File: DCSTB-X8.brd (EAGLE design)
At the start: 29 x 87 mm, 6 parts

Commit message: Changed board texts. Generated CAM files. Generated PDF schematics.
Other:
- board text added: "DCSTB-X8-0010 (c) Andriy Golovnya http://redscorp.net"
- board text removed: "DC-STB-X8-0010 (c) Andriy Golovnya http://redscorp.net"
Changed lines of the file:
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@@
 <drawing>
 <settings>
-<setting alwaysvectorfont="yes"/>
+<setting alwaysvectorfont="no"/>
 <setting verticaltext="up"/>
 </settings>
@@
 <circle x="15" y="4" radius="4.5" width="0.127" layer="51"/>
 <circle x="15" y="83" radius="4.5" width="0.127" layer="51"/>
-<text x="28" y="54" size="1.778" layer="22" font="vector" rot="MR270">DC-STB-X8-0010
+<text x="28" y="54" size="1.778" layer="22" font="vector" rot="MR270">DCSTB-X8-0010
 (c) Andriy Golovnya
 http://redscorp.net</text>

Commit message: Fixed QR code on x8 and x10 board. Generated CAM files.
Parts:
- moved LOGO2 1.00 mm to (11.0, 1.00)
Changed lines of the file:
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@@
 <element name="U$4" library="KF8500-Terminals" package="KF8500-8.5-2P" value="KF8500-8.5-2P" x="15" y="69" smashed="yes" rot="R90"/>
 <element name="LOGO1" library="_my_logos" package="MFDEC_L_10MM" value="MFDECLOGO_L_10MM" x="15" y="75" smashed="yes" rot="MR0"/>
-<element name="LOGO2" library="_my_logos" package="RSNURL_QR_10MM" value="RSNURL_QR_10MM" x="10" y="1" smashed="yes" rot="MR0"/>
+<element name="LOGO2" library="_my_logos" package="RSNURL_QR_10MM" value="RSNURL_QR_10MM" x="11" y="1" smashed="yes" rot="MR0"/>
 </elements>
 <signals>

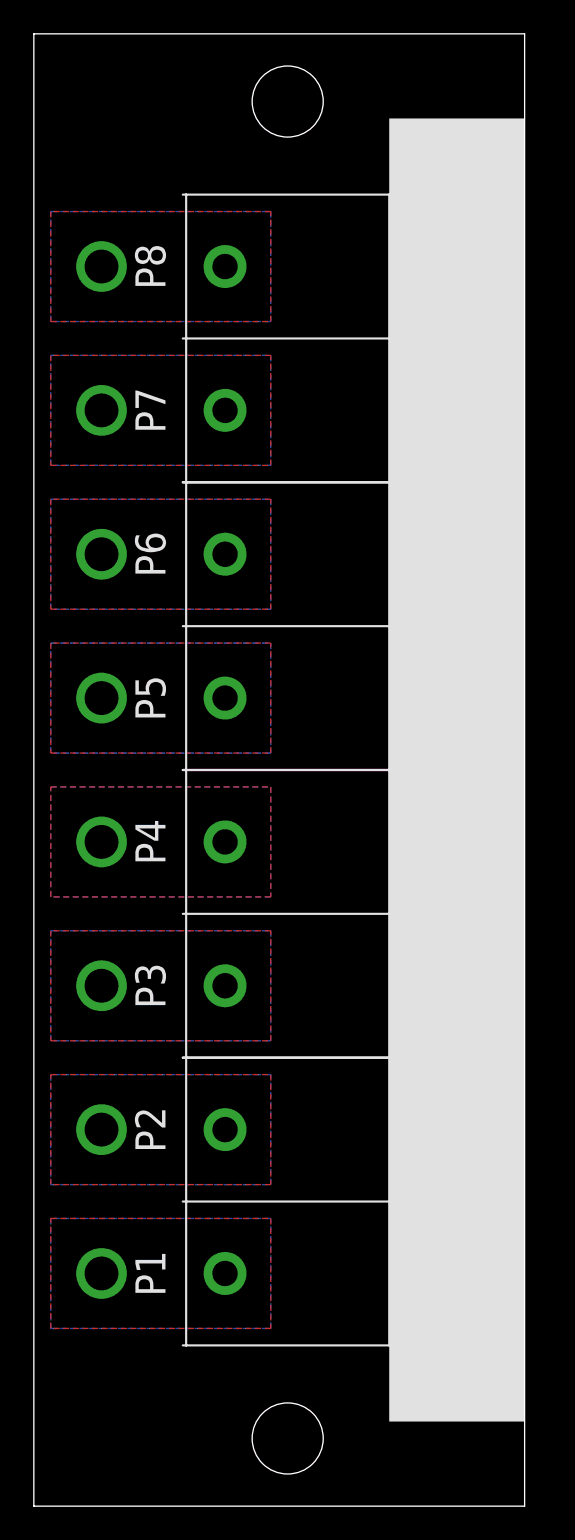
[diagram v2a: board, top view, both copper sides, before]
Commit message: Made boards a little bigger. Generated PNG preview. Generated CAM files.
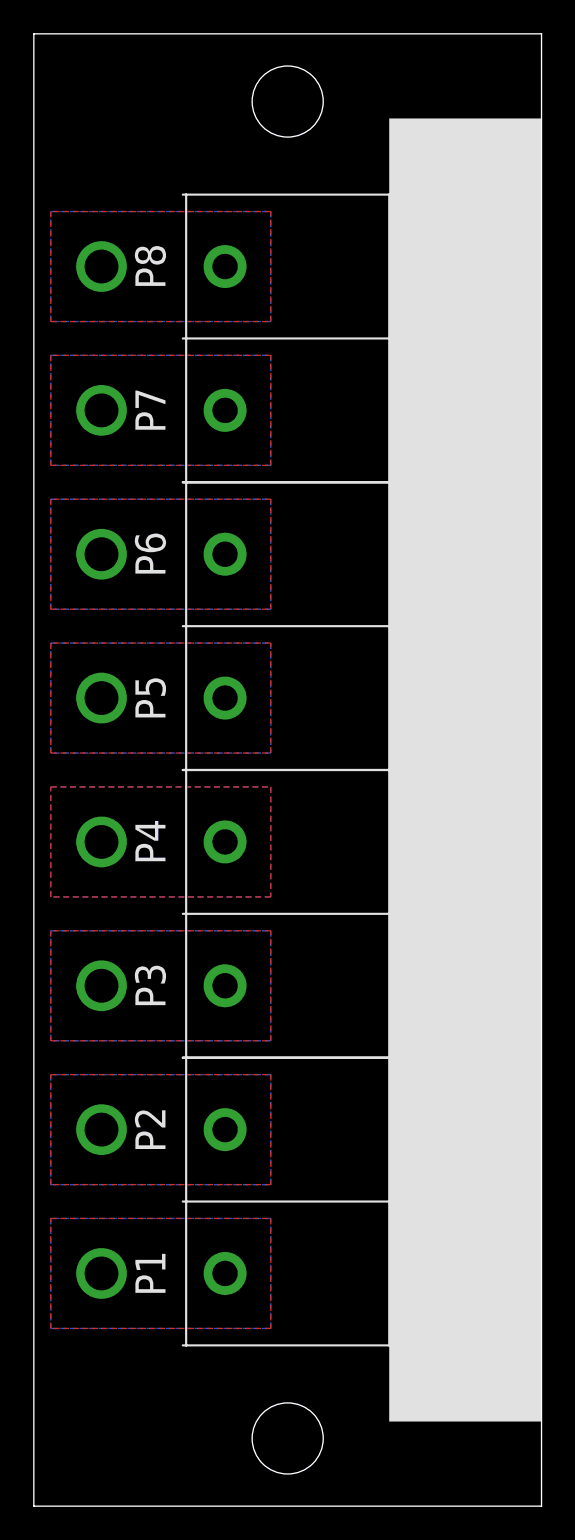
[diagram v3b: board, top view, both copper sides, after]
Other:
- board size 29 x 87 mm -> 30 x 87 mm
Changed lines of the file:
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@@
 <board>
 <plain>
-<wire x1="0" y1="0" x2="29" y2="0" width="0" layer="20"/>
-<wire x1="29" y1="0" x2="29" y2="87" width="0" layer="20"/>
-<wire x1="29" y1="87" x2="0" y2="87" width="0" layer="20"/>
+<wire x1="0" y1="0" x2="30" y2="0" width="0" layer="20"/>
+<wire x1="30" y1="0" x2="30" y2="87" width="0" layer="20"/>
+<wire x1="30" y1="87" x2="0" y2="87" width="0" layer="20"/>
 <wire x1="0" y1="87" x2="0" y2="0" width="0" layer="20"/>
 <hole x="15" y="4" drill="4.2"/>
@@
 <circle x="15" y="4" radius="4.5" width="0.127" layer="51"/>
 <circle x="15" y="83" radius="4.5" width="0.127" layer="51"/>
-<text x="28" y="54" size="1.778" layer="22" font="vector" rot="MR270">DCSTB-X8-0010
+<text x="29" y="54" size="1.778" layer="22" font="vector" rot="MR270">DCSTB-X8-0010
 (c) Andriy Golovnya
 http://redscorp.net</text>
-<rectangle x1="21" y1="5" x2="29" y2="82" layer="21"/>
+<rectangle x1="21" y1="5" x2="30" y2="82" layer="21"/>
 <text x="6" y="13.75" size="1.778" layer="21" font="vector" rot="R90" align="top-center">P1</text>
 <text x="6" y="22.25" size="1.778" layer="21" font="vector" rot="R90" align="top-center">P2</text>
